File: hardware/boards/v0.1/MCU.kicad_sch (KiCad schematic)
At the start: 38 parts, among them SW24 NRST, SW25 BOOT0, U1 BMDU, U18 STM32H743ZIT6, Y1 7E032768H01, Y4 X322525MOB4SI

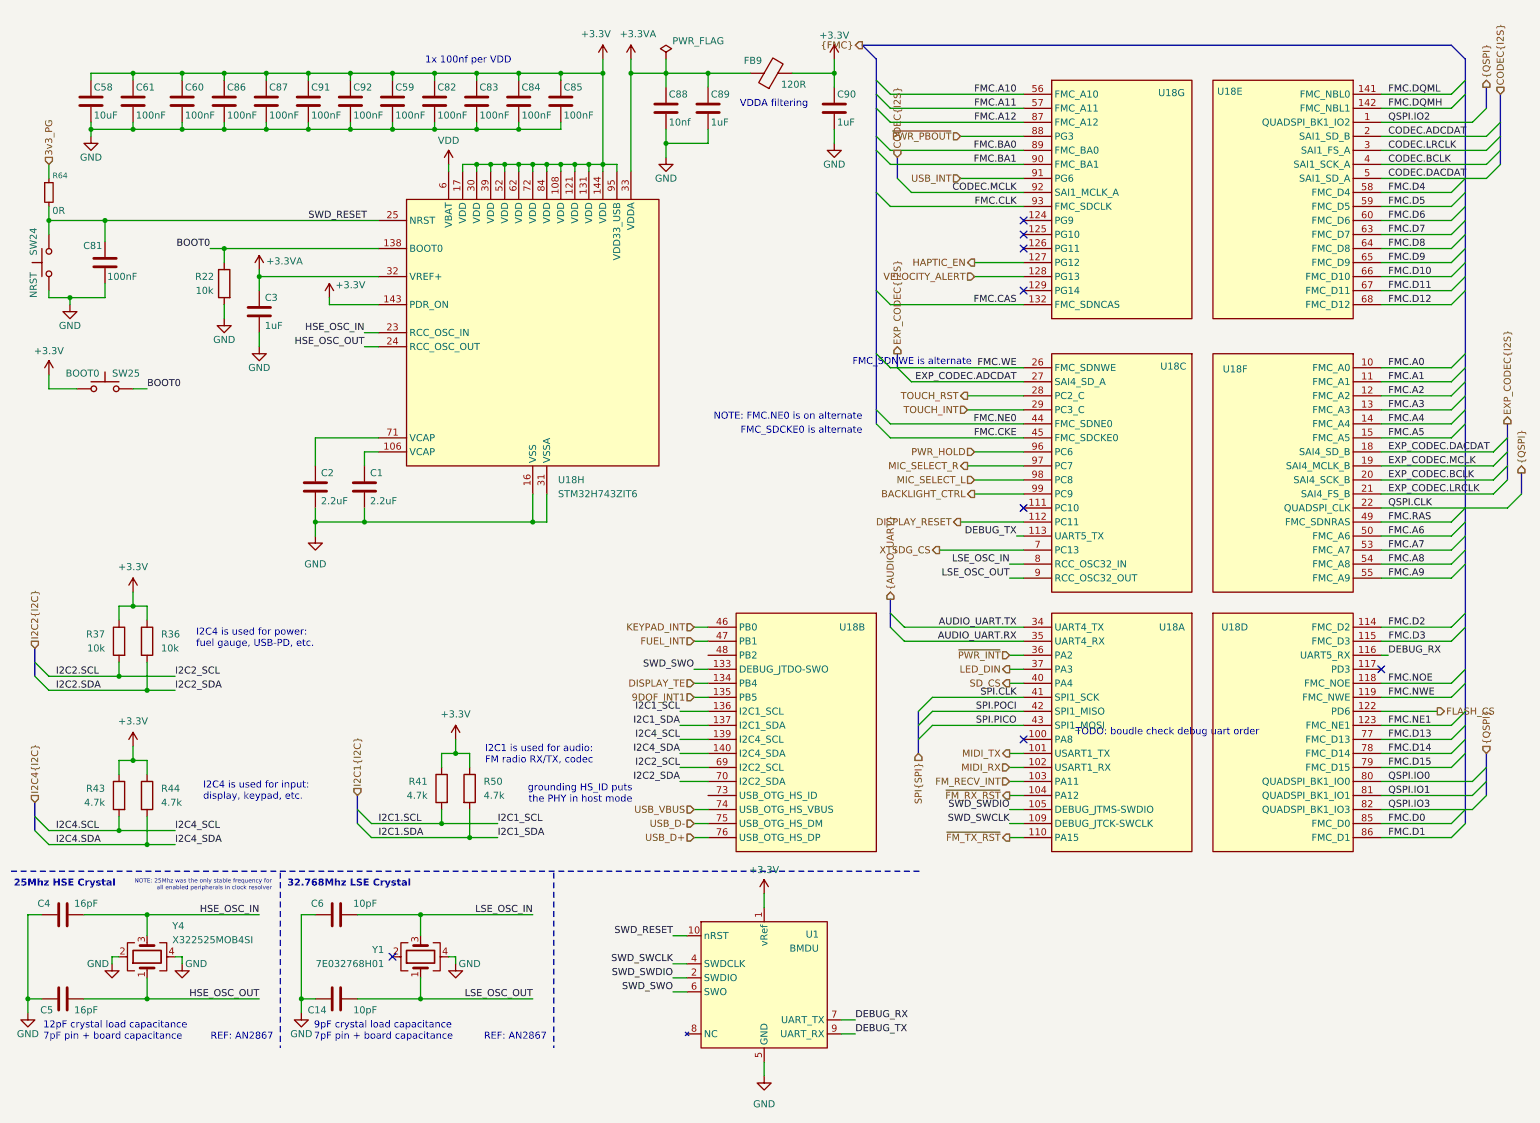
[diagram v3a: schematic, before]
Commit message: feat: various layout and routing adjustments
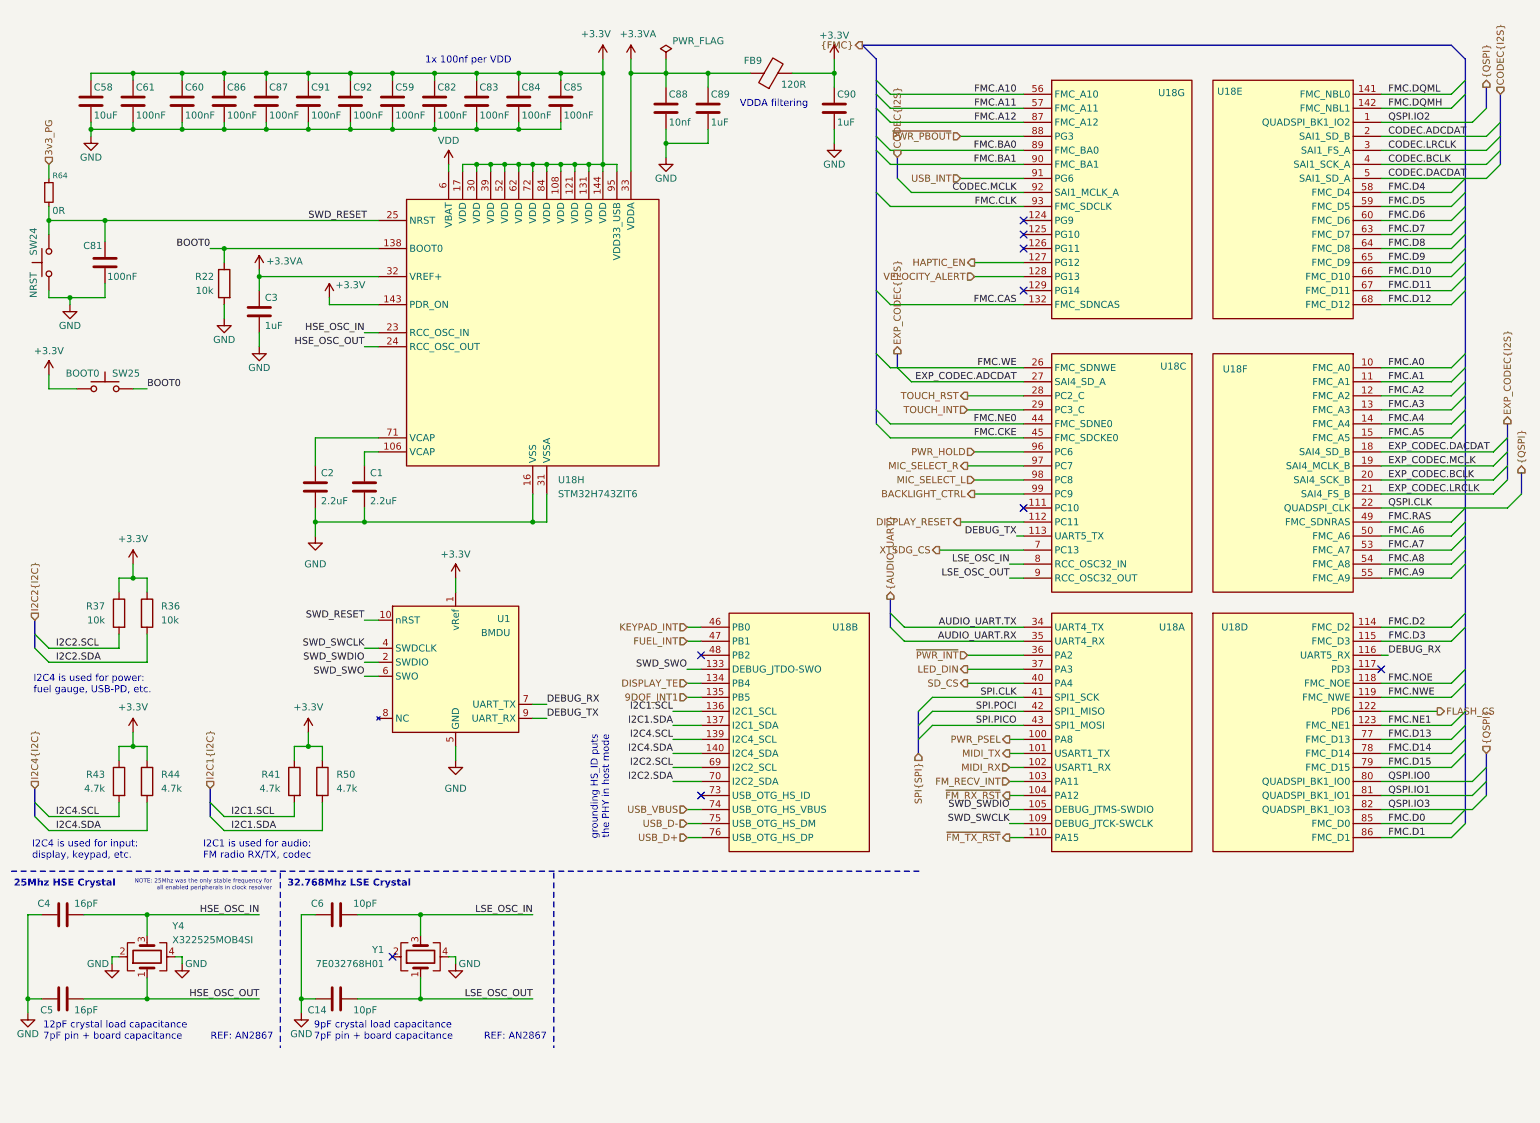
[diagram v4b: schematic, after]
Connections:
- net PWR_PSEL: now reaches U18.100 (PA8)
- no-connect marks 8 -> 9
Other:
- note removed: "FMC_SDCKE0 is alternate"
- note removed: "FMC_SDNWE is alternate"
- note removed: "NOTE: FMC.NE0 is on alternate"
- note removed: "TODO: boudle check debug uart order"
- moved on the sheet: R36, R37, R41, R43, R44, R50, U1, U18B

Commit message: chore: more DFM tweaks
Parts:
- C14, C6: JLC C1545 -> C32949
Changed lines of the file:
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@@
 			)
 		)
-		(property "JLC" "C1545"
+		(property "JLC" "C32949"
 			(at 71.12 173.99 0)
 			(effects
@@
 			)
 		)
-		(property "JLC" "C1545"
+		(property "JLC" "C32949"
 			(at 71.12 189.23 0)
 			(effects

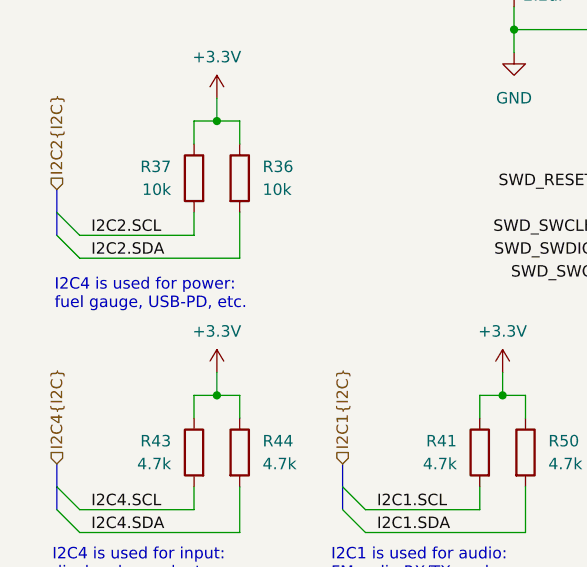
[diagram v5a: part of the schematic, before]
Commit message: feat: add pins in silkscreen, various DFM adjustments for JLC
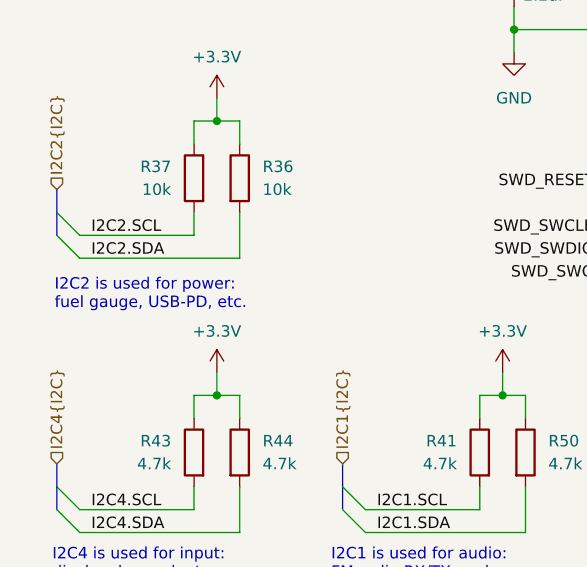
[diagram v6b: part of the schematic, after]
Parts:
- SW24, SW25: FT Rotation Offset (none) -> 90
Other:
- note added: "I2C2 is used for power: fuel gauge, USB-PD, etc."
- note removed: "I2C4 is used for power: fuel gauge, USB-PD, etc."
